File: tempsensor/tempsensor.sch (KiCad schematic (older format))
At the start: 64 parts, among them J1 USB_B_Micro, Q1 BC817, Q2 BC817, Q3 BC817, Q4 BSS806N, SW1 PW_OFF, SW2 PW_OFF, SW3 PW_ON, U2 ESP-12F, U3 24C16, U4 MCP73831-2-OT, U5 MCP9844, U6 MAX17620

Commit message: Finished layouting, exchanged two false diode packages, added protection diode to RTC reset line output, updated config button circuit.
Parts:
- added C2: 1u, Capacitor_SMD:C_0603_1608Metric, symbol Device:C
- added D6: SL03, Diode_SMD:D_SMF, symbol Device:D_Schottky
- added Q5: BC817, Package_TO_SOT_SMD:SOT-23, symbol Transistor_BJT:BC817
- added R20: 4K7, Resistor_SMD:R_0603_1608Metric, symbol Device:R
- added R23: 0R37, Resistor_SMD:R_0603_1608Metric, symbol Device:R
- added TP1: GPIO15, TestPoint:TestPoint_Pad_D1.0mm, symbol Connector:TestPoint
- D2, D3: footprint Diode_SMD:D_SMF -> Diode_SMD:D_SOD-123
- R7: value 10K -> 4K7
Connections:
- wire segments 201 -> 213
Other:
- moved on the sheet: D1, R8, SW1

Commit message: Created base schematic for MKW41 tempsensor, still need to finetune it.
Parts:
- removed C1: 10n, Capacitor_SMD:C_0603_1608Metric, symbol Device:C
- removed C10: 2u2, Capacitor_SMD:C_0603_1608Metric, symbol Device:C
- removed C11: 10u, Capacitor_SMD:C_0805_2012Metric, symbol Device:C
- removed C12, C2, C5, C9: 1u, Capacitor_SMD:C_0603_1608Metric, symbol Device:C
- removed C6: 100n, Capacitor_SMD:C_0603_1608Metric, symbol Device:C
- removed C7: 4u7, Capacitor_SMD:C_0805_2012Metric, symbol Device:C
- removed D1: LED, LED_SMD:LED_1210_3225Metric, symbol Device:LED
- removed D2, D3: SL03, Diode_SMD:D_SOD-123, symbol Device:D_Schottky
- removed D5: ZMM3V3, Diode_SMD:D_MiniMELF, symbol Device:D_Zener
- removed D6: SL03, Diode_SMD:D_SMF, symbol Device:D_Schottky
- removed L1: 1u, Inductor_SMD:L_1210_3225Metric, symbol Device:L
- removed Q1, Q2, Q3, Q5: BC817, Package_TO_SOT_SMD:SOT-23, symbol Transistor_BJT:BC817
- removed R10, R11, R12, R13, R14, R18, R19, R5, R6: 10K, Resistor_SMD:R_0603_1608Metric, symbol Device:R
- removed R16, R22, R3: 100K, Resistor_SMD:R_0603_1608Metric, symbol Device:R
- removed R17, R20, R7: 4K7, Resistor_SMD:R_0603_1608Metric, symbol Device:R
- removed R2: 430K, Resistor_SMD:R_0603_1608Metric, symbol Device:R
- removed R21: 313K, Resistor_SMD:R_0603_1608Metric, symbol Device:R
- removed R23: 0R37, Resistor_SMD:R_0603_1608Metric, symbol Device:R
- removed R8: 330, Resistor_SMD:R_0603_1608Metric, symbol Device:R
- removed R9: 2K, Resistor_SMD:R_0603_1608Metric, symbol Device:R
- removed TP7: DTR, TestPoint:TestPoint_Pad_D1.0mm, symbol Connector:TestPoint
- removed TP8: RTS, TestPoint:TestPoint_Pad_D1.0mm, symbol Connector:TestPoint
- removed U2: ESP-12F, RF_Module:ESP-12E, symbol RF_Module:ESP-12F
- removed U4: MCP73831-2-OT, Package_TO_SOT_SMD:SOT-23-5, symbol Battery_Management:MCP73831-2-OT
- removed U6: MAX17620, Package_DFN_QFN:DFN-8-1EP_2x2mm_P0.5mm_EP0.9x1.3mm, symbol tempsensor-rescue:MAX17620-Regulator_Switching
- added C?: 0,7p, symbol Device:C
- added C? (x2): 10p, symbol Device:C
- added C?: C, symbol Device:C
- added C?: 0.1u, symbol Device:C
- added C? (x2): 10u, symbol Device:C
- added C? (x4): 1u, symbol Device:C
- added C? (x5): 100n, symbol Device:C
- added C? (x2): 12p, symbol Device:C
- added C? (x2): 10n, symbol Device:C
- added D? (x2): LED, LED_SMD:LED_1210_3225Metric, symbol Device:LED
- added J?: Conn_ARM_JTAG_SWD_10, symbol Connector:Conn_ARM_JTAG_SWD_10
- added L?: 5,6n, symbol Device:L
- added L?: 10u, symbol Device:L_Core_Iron
- added L? (x2): 100n, symbol Device:L
- added Q? (x2): BSS806N, Package_TO_SOT_SMD:SOT-23, symbol Device:Q_NMOS_GSD
- added R?: 102K, symbol Device:R
- added R?: R, symbol Device:R
- added R? (x11): R, Resistor_SMD:R_0603_1608Metric, symbol Device:R
- added U?: MKW41Z512VHT, Package_DFN_QFN:NXP_LQFN-48-1EP_7x7mm_P0.5mm_EP3.5x3.5mm_16xMask0.45x0.45_ThermalVias, symbol MCU_NXP_Kinetis:MKW41Z512VHT
- added U?: BQ24012, Package_SON:VSON-10-1EP_3x3mm_P0.5mm_EP1.65x2.4mm_ThermalVias, symbol Battery_Management:BQ24012
- added Y?: 32MHz 10PPM SMT 2.0x1.6mm 10PF, symbol Device:Crystal_GND24
- added Y?: 32.768KHz 20PPM 3.2x1.5mm 7PF, symbol Device:Crystal
- C4: value 4u7 -> 1u; footprint Capacitor_SMD:C_0805_2012Metric -> (none)
- R1, R4: value 1K -> 2K2
- R15: value 470 -> R
- SW1: value PW_OFF -> RST
- SW2: value PW_OFF -> ~INT
- TP1: value GPIO15 -> XTAL_OUT
- TP16: value TMP -> ~TMP_INT
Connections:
- net labels added: +1V8, SWD_CLK, SWD_IO, TMP0_CH0, TMP0_CH1, TMP0_CH2, TMP0_CH3, VDDA, VDD_1P5V, VDD_MCU, VDD_RF, VREFHVREF_OUT, XTAL_OUT, ~BTN_INT, ~CHG_DONE, ~CHG_PG, ~CHG_RUN, ~MCU_RST, ~TMP_INT
- net labels removed: CONF, DTR, EN, GPIO0, GPIO2, RTS
- wire segments 213 -> 272
- no-connect marks 12 -> 5
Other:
- note added: "50 Ohm controlled impedane line"
- note added: "DNP if internal pullups of MKW41 can be used\nin all of its power states"
- note added: "DNP\nFor V2, check if the internal Pullups are \nactive in VLLS and LLS power modes"
- note added: "For V2, check if the internal Pullups are \nactive in VLLS and LLS power modes"
- note added: "TWI only 100kHz since EEPROM and tempsensor can only handle that at 1,8V!"
- note added: "This matching network transforms device impedance to 50 Ohms\nPlace as close to device as possible"
- note added: "Use event output to wake up MCU\nThis even eliminates periodic wake up\nMCU has internal RTC to wake up to heating program timechanges to re-set temp limits"
- note removed: "Battery Disconnect\nWhen charger is connected,\nVBUS voltage is higher than +BATT\nLoad still supplied from\nUSB, but not from battery"
- note removed: "ESP Bootstrapping Circuit"
- note removed: "ESP-12F"
- note removed: "ISP programming"
- note removed: "Selfkill for ESP\nif GPIO15 is pulled high, a NMOS discharges ~UVSLO~, \ndisabling the DC/DC converter.\nTo avoid turning the converter back on when the ESP \nis browning out and not driving the MOS that strong \nany more, a fairly large capacitor (C12) on ~UVSLO~ is \nused to prevent a too fast recharge and restart of \nthe converter"
- note removed: "Step-Down battery to 3,3V\n(or lower)"
- moved on the sheet: +BATT1, C3, C4, C8, D4, GND1, J1, Q4, R1, R15, R4, SW1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

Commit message: Finished Tempsensor schematic based on MKW41Z. Many footprints not associated yet.
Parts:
- removed +BATT1: +BAT, TestPoint:TestPoint_Pad_4.0x4.0mm, symbol Connector:TestPoint
- removed C3: 100n, Capacitor_SMD:C_0603_1608Metric, symbol Device:C
- removed C4, C? (x4): 1u, symbol Device:C
- removed C8: 10n, Capacitor_SMD:C_0603_1608Metric, symbol Device:C
- removed C? (x2): 10u, symbol Device:C
- removed C? (x5): 100n, symbol Device:C
- removed C? (x2): 12p, symbol Device:C
- removed C? (x2): 10n, symbol Device:C
- removed D4, D? (x2): LED, LED_SMD:LED_1210_3225Metric, symbol Device:LED
- removed GND1: GND, TestPoint:TestPoint_Pad_4.0x4.0mm, symbol Connector:TestPoint
- removed J1: USB_B_Micro, myfootprints:USB-Mini-B_Wuerth_651005136521_Horizontal, symbol Connector:USB_B_Micro
- removed J?: Conn_ARM_JTAG_SWD_10, symbol Connector:Conn_ARM_JTAG_SWD_10
- removed L? (x2): 100n, symbol Device:L
- removed Q4, Q? (x2): BSS806N, Package_TO_SOT_SMD:SOT-23, symbol Device:Q_NMOS_GSD
- removed R1, R4: 2K2, Resistor_SMD:R_0603_1608Metric, symbol Device:R
- removed R15, R? (x11): R, Resistor_SMD:R_0603_1608Metric, symbol Device:R
- removed R?: R, symbol Device:R
- removed SW1: RST, Button_Switch_THT:SW_PUSH_6mm_H5mm, symbol Switch:SW_Push
- removed SW2: ~INT, Button_Switch_THT:SW_PUSH_6mm_H5mm, symbol Switch:SW_Push
- removed TP12: 3V3, TestPoint:TestPoint_Pad_D1.0mm, symbol Connector:TestPoint
- removed TP13: ~UVSLO, TestPoint:TestPoint_Pad_D1.0mm, symbol Connector:TestPoint
- removed TP14: VDC, TestPoint:TestPoint_Pad_D1.0mm, symbol Connector:TestPoint
- removed TP16: ~TMP_INT, TestPoint:TestPoint_Pad_D1.0mm, symbol Connector:TestPoint
- removed TP3: VBUS, TestPoint:TestPoint_Pad_D1.0mm, symbol Connector:TestPoint
- removed TP4: GND, TestPoint:TestPoint_Pad_D1.0mm, symbol Connector:TestPoint
- removed TP5: RXD, TestPoint:TestPoint_Pad_D1.0mm, symbol Connector:TestPoint
- removed TP6: TXD, TestPoint:TestPoint_Pad_D1.0mm, symbol Connector:TestPoint
- removed TP9: ~RST, TestPoint:TestPoint_Pad_D1.0mm, symbol Connector:TestPoint
- removed U3: 24C16, Package_SO:SOIC-8_3.9x4.9mm_P1.27mm, symbol Memory_EEPROM:CAT24C128
- removed U5: MCP9844, Package_DFN_QFN:DFN-8-1EP_3x2mm_P0.5mm_EP1.36x1.46mm, symbol Sensor_Temperature:MCP9844x-xMN
- removed U?: BQ24012, Package_SON:VSON-10-1EP_3x3mm_P0.5mm_EP1.65x2.4mm_ThermalVias, symbol Battery_Management:BQ24012
- added AE1: Antenna_Shield, RF_Antenna:Texas_SWRA117D_2.4GHz_Left, symbol Device:Antenna_Shield
- added J1: Conn_01x14, Connector_PinHeader_2.54mm:PinHeader_1x14_P2.54mm_Vertical, symbol Connector_Generic:Conn_01x14
- added SW1: SW_DIP_x06, symbol Switch:SW_DIP_x06
- Y2: renamed from Y?; footprint (none) -> Crystal:Crystal_SMD_3215-2Pin_3.2x1.5mm
- gave numbers to parts that had none: 10
- renumbered SW3 to SW2
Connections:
- net +1V8: now also J1.1 (Pin_1); no longer U1.20 (VDD_0), U1.44 (VDD_1)
- net +BATT: now also J1.2 (Pin_2)
- net GND: now also AE1.2 (Shield), J1.13 (Pin_13), J1.14 (Pin_14), SW1.10, SW1.11, SW1.12, SW1.7, SW1.8, SW1.9
- net TMP0_CH2: now also J1.9 (Pin_9), SW1.3
- net TMP0_CH3: now also J1.10 (Pin_10), SW1.4
- net ~BTN_INT: now also U1.6 (PTA18), J1.6 (Pin_6); no longer U1.5 (PTA17)
- net ~CHG_PG: now also U1.41 (PTC5); no longer U1.48 (PTC19)
- net PTB2: now reaches U1.18 (PTB2)
- net PTB2: now also J1.7 (Pin_7), SW1.1
- net PTB3: now reaches U1.19 (PTB3)
- net PTB3: now also J1.8 (Pin_8), SW1.2
- net PTC1: now reaches U1.37 (PTC1)
- net PTC1: now also J1.3 (Pin_3)
- net PTA16: now reaches U1.4 (PTA16)
- net PTA16: now also J1.11 (Pin_11), SW1.5
- net PTC4: now reaches U1.40 (PTC4)
- net PTC4: now also J1.4 (Pin_4)
- net LPUART0_RX: now reaches U1.42 (PTC6)
- net LPUART0_TX: now reaches U1.43 (PTC7)
- net at C4.1: now also AE1.1 (A)
- net VDD_1P5V renamed +1V5
- new net PTA17: J1.12 (Pin_12), SW1.6, U1.5 (PTA17)
- new net PTC19: J1.5 (Pin_5), U1.48 (PTC19)
- new net VDD_MCU: U1.20 (VDD_0), U1.44 (VDD_1)
- no-connect marks 5 -> 0
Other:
- note added: "1V8 comes from MCU regulator and cannot handle large loads!"
- note added: "DIP switch for easy configuration,\nuse internal GPIO pullups.\nDon't forget to open switches if pins are used otherwise"
- note added: "PTC1 & PTC19 carry I2C0 bus"
- note added: "TMP1 available on these two pins"
- note removed: "Battery Charger Circuit"
- note removed: "Battery Connector"
- note removed: "DNP if internal pullups of MKW41 can be used\nin all of its power states"
- note removed: "DNP\nFor V2, check if the internal Pullups are \nactive in VLLS and LLS power modes"
- note removed: "EEPROM for off-ESP config"
- note removed: "For V2, check if the internal Pullups are \nactive in VLLS and LLS power modes"
- note removed: "MCP9844 Tempsensor"
- note removed: "TWI only 100kHz since EEPROM and tempsensor can only handle that at 1,8V!"
- note removed: "Testpointsfor verification and programming"
- note removed: "USB Connector\nfor charging only"
- note removed: "Use event output to wake up MCU\nThis even eliminates periodic wake up\nMCU has internal RTC to wake up to heating program timechanges to re-set temp limits"
- note removed: "e-Lab"

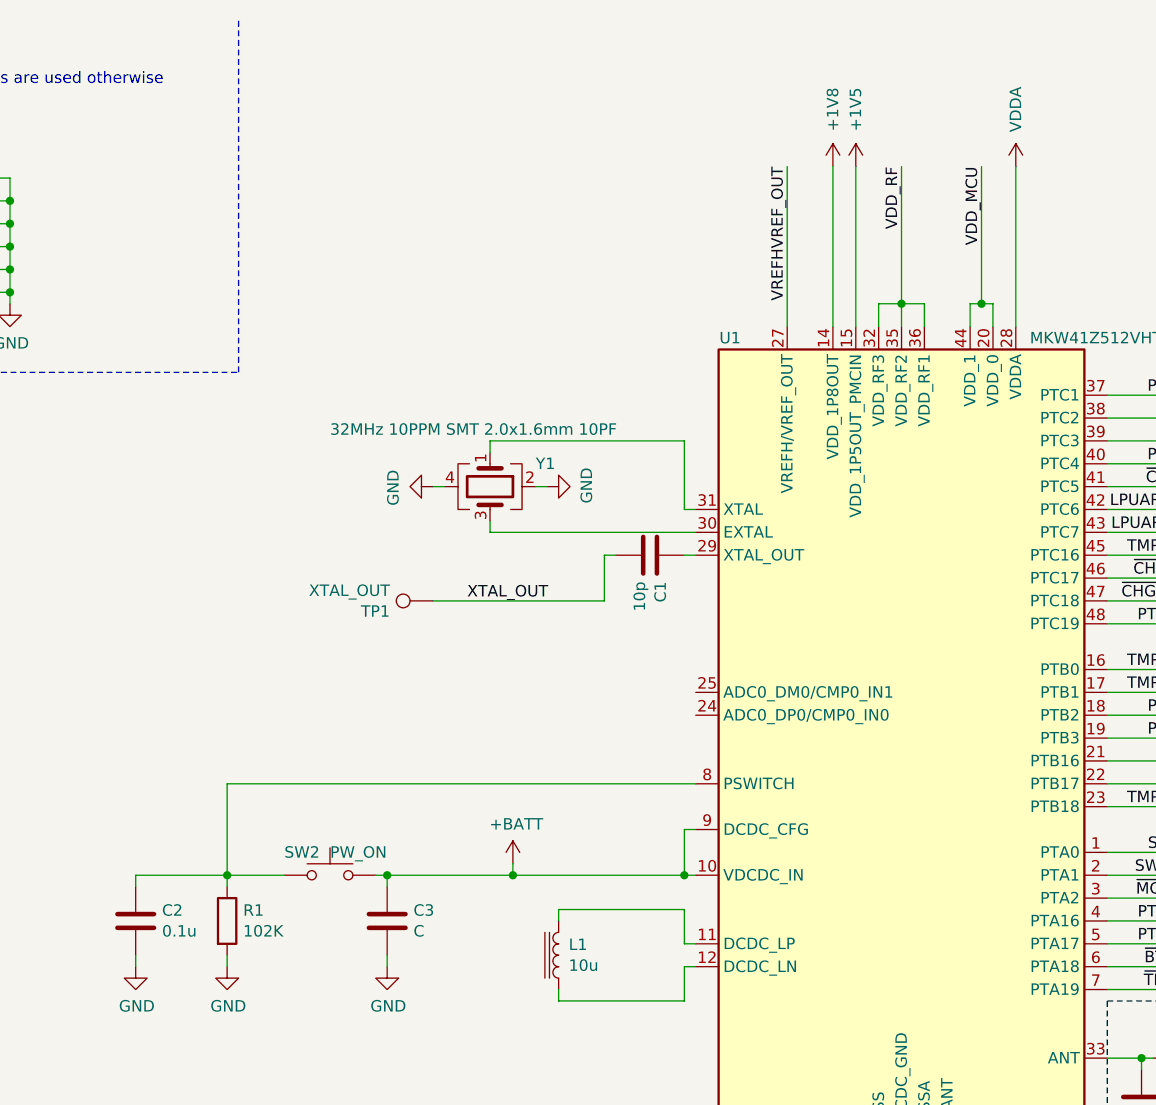
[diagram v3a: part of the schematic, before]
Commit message: Added footprints to tempsensor.
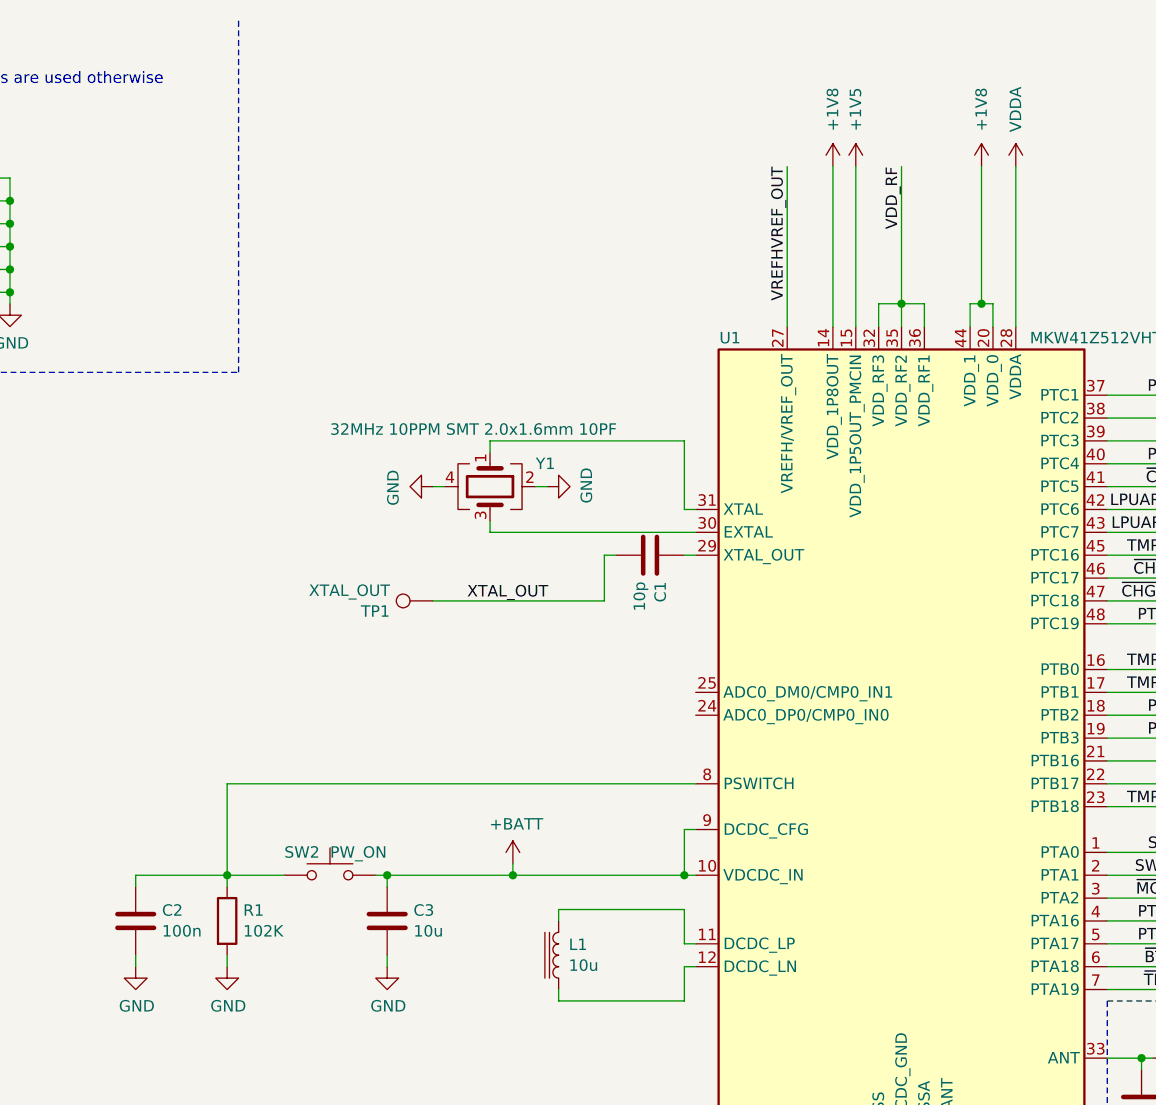
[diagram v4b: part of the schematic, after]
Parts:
- C1, C4, C5: footprint (none) -> Capacitor_SMD:C_0402_1005Metric
- C2: value 0.1u -> 100n; footprint (none) -> Capacitor_SMD:C_0402_1005Metric
- C3: value C -> 10u; footprint (none) -> Capacitor_SMD:C_0603_1608Metric
- J1: footprint Connector_PinHeader_2.54mm:PinHeader_1x14_P2.54mm_Vertical -> Connector_PinHeader_2.54mm:PinHeader_2x07_P2.54mm_Vertical
- L1: footprint (none) -> Inductor_SMD:L_Wuerth_MAPI-3012; MFP (none) -> VLS3012CX-100M-1
- L2: footprint (none) -> Inductor_SMD:L_0402_1005Metric
- R1: footprint (none) -> Resistor_SMD:R_0402_1005Metric
- SW1: footprint (none) -> Button_Switch_SMD:SW_DIP_SPSTx06_Slide_Omron_A6S-610x_W8.9mm_P2.54mm
- U1: footprint Package_DFN_QFN:NXP_LQFN-48-1EP_7x7mm_P0.5mm_EP3.5x3.5mm_16xMask0.45x0.45_ThermalVias -> Package_DFN_QFN:NXP_LQFN-48-1EP_7x7mm_P0.5mm_EP3.5x3.5mm_16xMask0.45x0.45
- Y1: footprint (none) -> Crystal:Crystal_SMD_2016-4Pin_2.0x1.6mm
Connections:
- net VDD_MCU is gone; now on net +1V8: U1.20 (VDD_0), U1.44 (VDD_1)
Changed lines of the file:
@@
 F 0 "U1" H 4950 5400 50  0000 C CNN
 F 1 "MKW41Z512VHT" H 6550 5400 50  0000 C CNN
-F 2 "Package_DFN_QFN:NXP_LQFN-48-1EP_7x7mm_P0.5mm_EP3.5x3.5mm_16xMask0.45x0.45_ThermalVias" H 5650 3650 50  0001 C CNN
+F 2 "Package_DFN_QFN:NXP_LQFN-48-1EP_7x7mm_P0.5mm_EP3.5x3.5mm_16xMask0.45x0.45" H 5650 3650 50  0001 C CNN
 F 3 "https://www.nxp.com/docs/en/data-sheet/MKW41Z512.pdf" H 5700 3550 50  0001 C CNN
 	1    5700 3650
@@
 F 0 "Y1" V 3800 2750 50  0000 L CNN
 F 1 "32MHz 10PPM SMT 2.0x1.6mm 10PF" V 3650 1850 50  0000 L CNN
-F 2 "" H 3900 2550 50  0001 C CNN
+F 2 "Crystal:Crystal_SMD_2016-4Pin_2.0x1.6mm" H 3900 2550 50  0001 C CNN
 F 3 "~" H 3900 2550 50  0001 C CNN
 	1    3900 2550
@@
 F 0 "C5" H 6865 5296 50  0000 L CNN
 F 1 "0,7p" H 6865 5205 50  0000 L CNN
-F 2 "" H 6788 5100 50  0001 C CNN
+F 2 "Capacitor_SMD:C_0402_1005Metric" H 6788 5100 50  0001 C CNN
 F 3 "~" H 6750 5250 50  0001 C CNN
 	1    6750 5250
@@
 F 0 "L2" V 7140 5050 50  0000 C CNN
 F 1 "5,6n" V 7049 5050 50  0000 C CNN
-F 2 "" H 6950 5050 50  0001 C CNN
+F 2 "Inductor_SMD:L_0402_1005Metric" H 6950 5050 50  0001 C CNN
 F 3 "~" H 6950 5050 50  0001 C CNN
 	1    6950 5050
@@
 F 0 "C4" V 7598 5050 50  0000 C CNN
 F 1 "10p" V 7689 5050 50  0000 C CNN
-F 2 "" H 7888 4900 50  0001 C CNN
+F 2 "Capacitor_SMD:C_0402_1005Metric" H 7888 4900 50  0001 C CNN
 F 3 "~" H 7850 5050 50  0001 C CNN
 	1    7850 5050
@@
 F 0 "L1" H 4156 4554 50  0000 R CNN
 F 1 "10u" H 4156 4645 50  0000 R CNN
-F 2 "" H 4200 4600 50  0001 C CNN
+F 2 "Inductor_SMD:L_Wuerth_MAPI-3012" H 4200 4600 50  0001 C CNN
 F 3 "~" H 4200 4600 50  0001 C CNN
+F 4 "VLS3012CX-100M-1" H 4200 4600 50  0001 C CNN "MFP"
 	1    4200 4600
 	-1   0    0    1
@@
 P 3450 4450
 F 0 "C3" H 3565 4496 50  0000 L CNN
-F 1 "C" H 3565 4405 50  0000 L CNN
-F 2 "" H 3488 4300 50  0001 C CNN
+F 1 "10u" H 3565 4405 50  0000 L CNN
+F 2 "Capacitor_SMD:C_0603_1608Metric" H 3488 4300 50  0001 C CNN
 F 3 "~" H 3450 4450 50  0001 C CNN
 	1    3450 4450
@@
 P 2350 4450
 F 0 "C2" H 2465 4496 50  0000 L CNN
-F 1 "0.1u" H 2465 4405 50  0000 L CNN
-F 2 "" H 2388 4300 50  0001 C CNN
+F 1 "100n" H 2465 4405 50  0000 L CNN
+F 2 "Capacitor_SMD:C_0402_1005Metric" H 2388 4300 50  0001 C CNN
 F 3 "~" H 2350 4450 50  0001 C CNN
 	1    2350 4450
@@
 F 0 "R1" H 2820 4496 50  0000 L CNN
 F 1 "102K" H 2820 4405 50  0000 L CNN
-F 2 "" V 2680 4450 50  0001 C CNN
+F 2 "Resistor_SMD:R_0402_1005Metric" V 2680 4450 50  0001 C CNN
 F 3 "~" H 2750 4450 50  0001 C CNN
 	1    2750 4450
@@
 Wire Wire Line
 	6100 1750 6100 1850
-Text Label 6050 1150 3    50   ~ 0
-VDD_MCU
 Text Label 5200 1150 3    50   ~ 0
 VREFHVREF_OUT
@@
 F 0 "C1" H 4715 2896 50  0000 L CNN
 F 1 "10p" H 4715 2805 50  0000 L CNN
-F 2 "" H 4638 2700 50  0001 C CNN
+F 2 "Capacitor_SMD:C_0402_1005Metric" H 4638 2700 50  0001 C CNN
 F 3 "~" H 4600 2850 50  0001 C CNN
 	1    4600 2850
@@
 Wire Wire Line
 	7050 4650 6600 4650
-Text Label 1000 6350 2    50   ~ 0
-PTC1
-Text Label 1000 6450 2    50   ~ 0
-PTC4
 Text Label 1000 7050 2    50   ~ 0
 TMP0_CH3
@@
 Wire Wire Line
 	6600 3050 7050 3050
-Text Label 1000 6550 2    50   ~ 0
-PTC19
 Text Notes 1300 6400 0    50   ~ 0
 PTC1 & PTC19 carry I2C0 bus
@@
 F 0 "SW1" H 1450 2067 50  0000 C CNN
 F 1 "SW_DIP_x06" H 1450 1976 50  0000 C CNN
-F 2 "" H 1450 1500 50  0001 C CNN
+F 2 "Button_Switch_SMD:SW_DIP_SPSTx06_Slide_Omron_A6S-610x_W8.9mm_P2.54mm" H 1450 1500 50  0001 C CNN
 F 3 "~" H 1450 1500 50  0001 C CNN
 	1    1450 1500
@@
 Text Notes 550  800  0    50   ~ 0
 DIP switch for easy configuration,\nuse internal GPIO pullups.\nDon't forget to open switches if pins are used otherwise
-$Comp
-L Connector_Generic:Conn_01x14 J1
-U 1 1 5F9F7615
-P 1200 6750
-F 0 "J1" H 1280 6742 50  0000 L CNN
-F 1 "Conn_01x14" H 1280 6651 50  0000 L CNN
-F 2 "Connector_PinHeader_2.54mm:PinHeader_1x14_P2.54mm_Vertical" H 1200 6750 50  0001 C CNN
-F 3 "~" H 1200 6750 50  0001 C CNN
-	1    1200 6750
-	1    0    0    -1
-$EndComp
 $Comp
 L power:+1V8 #PWR015
@@
 Wire Wire Line
 	12100 3000 12600 3000
+Text Label 1000 6550 2    50   ~ 0
+PTC19
+Text Label 1000 6450 2    50   ~ 0
+PTC4
+$Comp
+L Connector_Generic:Conn_01x14 J1
+U 1 1 5F9F7615
+P 1200 6750
+F 0 "J1" H 1280 6742 50  0000 L CNN
+F 1 "Conn_01x14" H 1280 6651 50  0000 L CNN
+F 2 "Connector_PinHeader_2.54mm:PinHeader_2x07_P2.54mm_Vertical" H 1200 6750 50  0001 C CNN
+F 3 "~" H 1200 6750 50  0001 C CNN
+	1    1200 6750
+	1    0    0    -1
+$EndComp
+Text Label 1000 6350 2    50   ~ 0
+PTC1
+$Comp
+L power:+1V8 #PWR0101
+U 1 1 5FE7600F
+P 6050 1150
+F 0 "#PWR0101" H 6050 1000 50  0001 C CNN
+F 1 "+1V8" V 6050 1400 50  0000 C CNN
+F 2 "" H 6050 1150 50  0001 C CNN
+F 3 "" H 6050 1150 50  0001 C CNN
+	1    6050 1150
+	1    0    0    -1
+$EndComp
 $EndSCHEMATC
